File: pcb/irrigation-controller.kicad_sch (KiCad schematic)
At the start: 7 parts, among them J1 ZL262-40DG, J2 KFG-2EDGR-5.08-9P, X1 5V, X2 12V

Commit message: Update resistor values based on availability
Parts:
- R10: value 1.5K -> 1.1K; CID 100.327.80 -> 100.011.53
- R9: value 4.3K -> 3.9K; CID 100.316.93 -> 100.014.54
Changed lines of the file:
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@@
 			)
 		)
-		(property "Value" "1.5K"
+		(property "Value" "1.1K"
 			(at 227.33 107.9499 0)
 			(effects
@@
 			)
 		)
-		(property "CID" "100.327.80"
+		(property "CID" "100.011.53"
 			(at 224.79 106.68 0)
 			(effects
@@
 			)
 		)
-		(property "Value" "4.3K"
+		(property "Value" "3.9K"
 			(at 227.33 97.7899 0)
 			(effects
@@
 			)
 		)
-		(property "CID" "100.316.93"
+		(property "CID" "100.014.54"
 			(at 224.79 96.52 0)
 			(effects

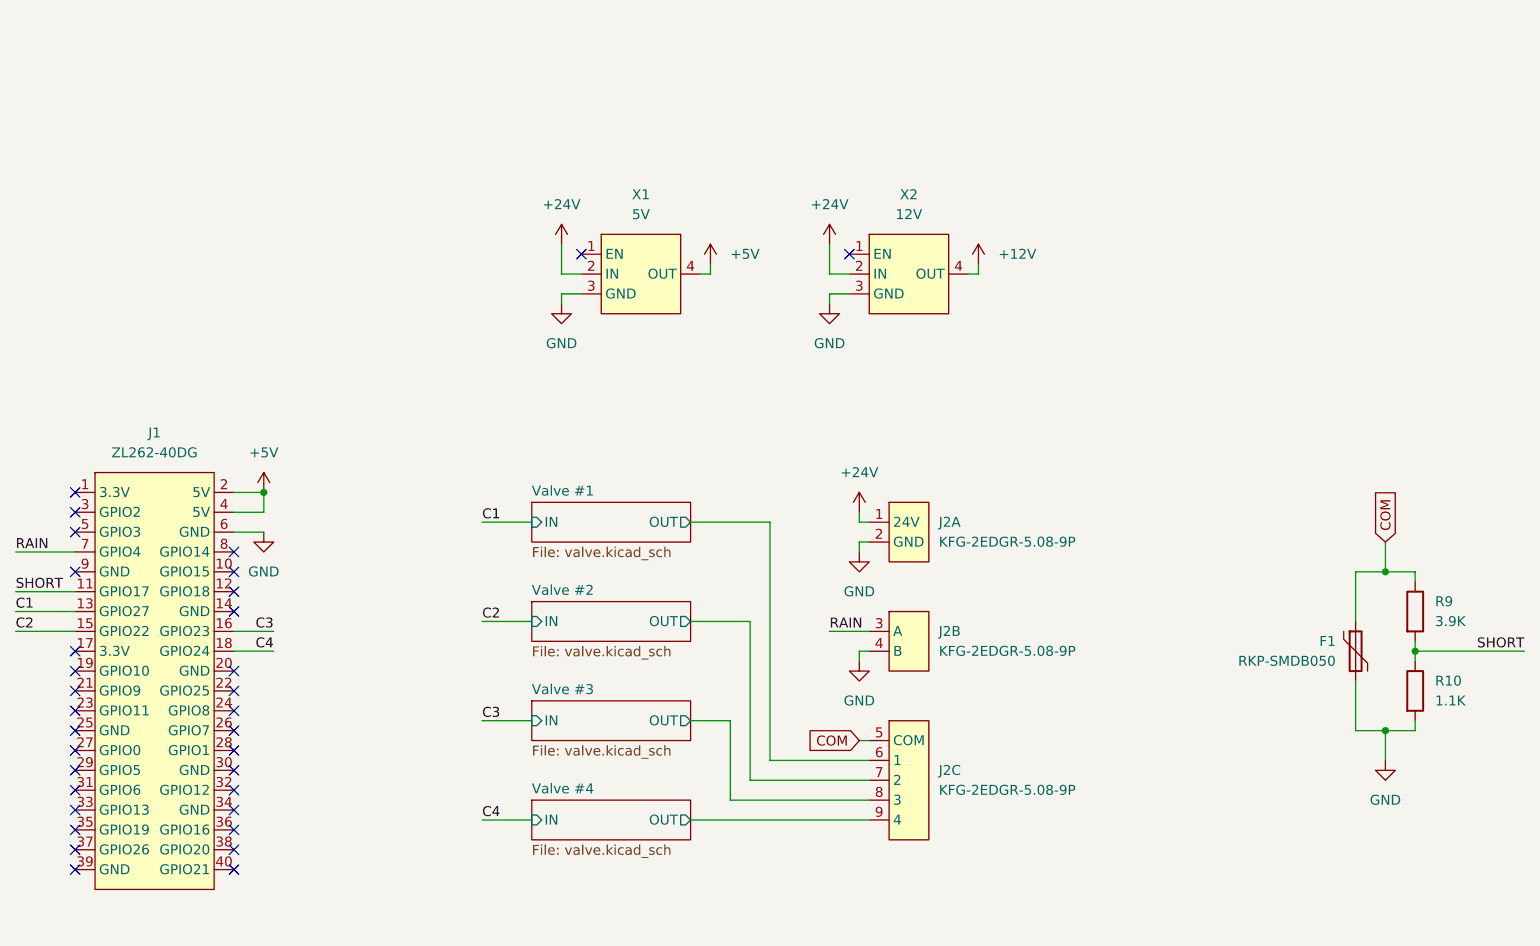
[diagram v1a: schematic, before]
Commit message: Change terminal, add another output, add hardware debouncing
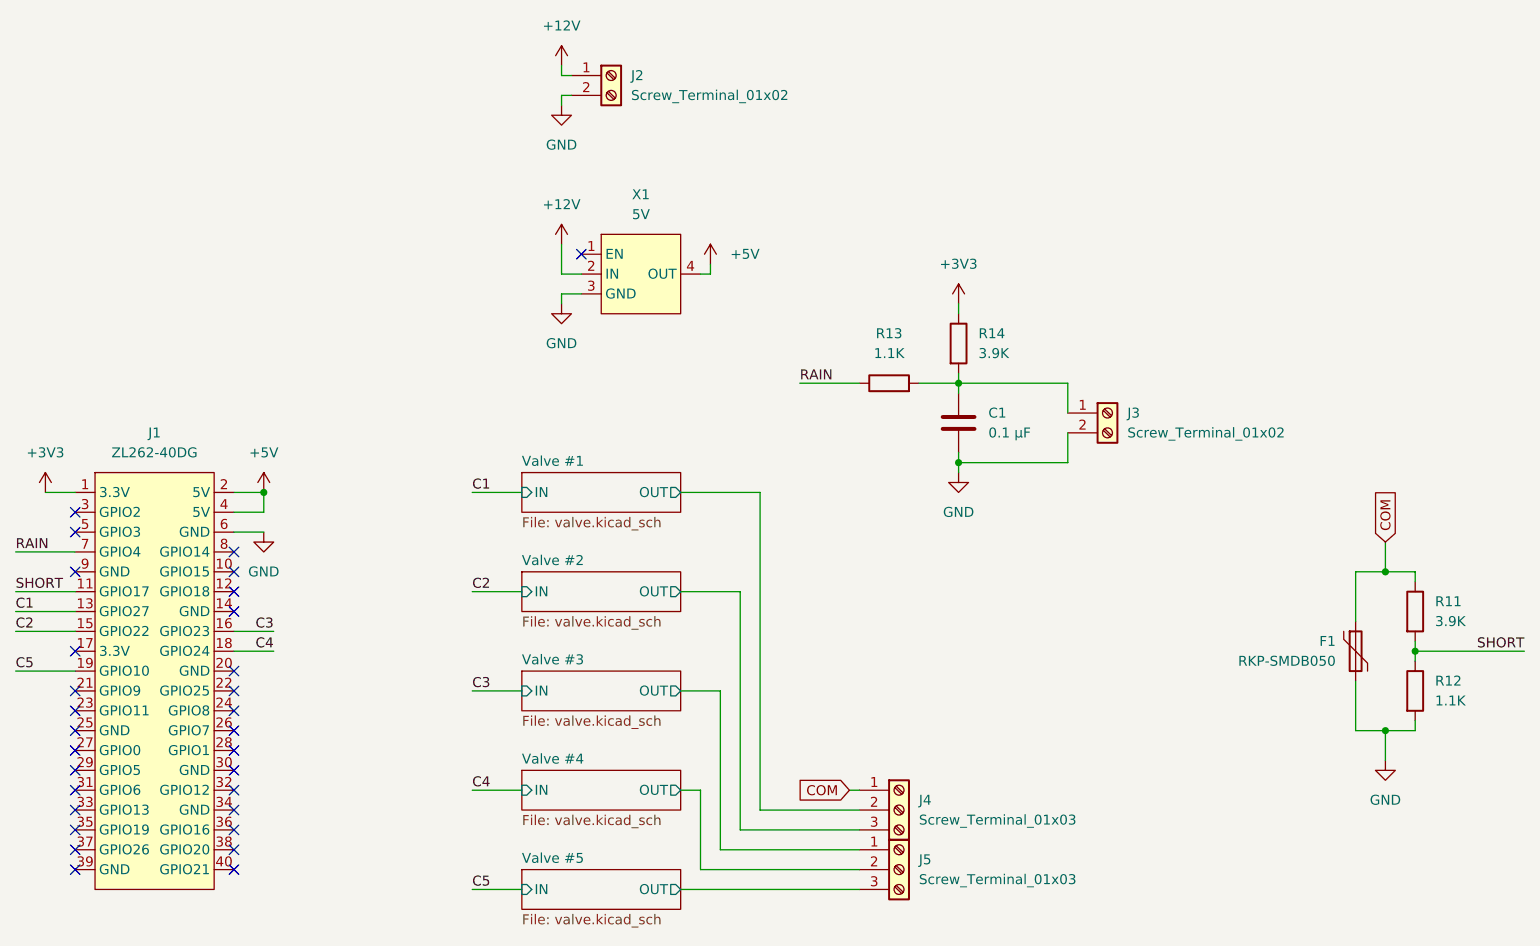
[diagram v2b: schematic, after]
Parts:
- removed J2: KFG-2EDGR-5.08-9P, Irrigation_Controller:KFG-2EDGR-5.08-9P, symbol Irrigation_Controller:Irrigation_Controller_Connector
- removed X2: 12V, Irrigation_Controller:STDN-3A24-ADJ, symbol Irrigation_Controller:STDN-3A24-ADJ
- added C1: 0.1 µF, Capacitor_SMD:C_0805_2012Metric, symbol Device:C
- added J2, J3: Screw_Terminal_01x02, Irrigation_Controller:MX5-2P-BK, symbol Connector:Screw_Terminal_01x02
- added J4, J5: Screw_Terminal_01x03, Irrigation_Controller:MX5-3P-BK, symbol Connector:Screw_Terminal_01x03
- added R13: 1.1K, Resistor_SMD:R_0805_2012Metric, symbol Device:R
- added R14: 3.9K, Resistor_SMD:R_0805_2012Metric, symbol Device:R
- renumbered R9 to R11, R10 to R12
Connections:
- net +24V is gone; now on net +12V: X1.2 (IN)
- net +12V: now also J2.1 (Pin_1)
- net COM: now also J4.1 (Pin_1)
- net GND: now also C1.2, J2.2 (Pin_2), J3.2 (Pin_2)
- net RAIN: now also R13.1
- net Valve #1/OUT: now also J4.2 (Pin_2)
- net Valve #2/OUT: now also J4.3 (Pin_3)
- net Valve #3/OUT: now also J5.1 (Pin_1)
- net Valve #4/OUT: now also J5.2 (Pin_2)
- net +3V3: now reaches J1.1 (3.3V)
- net +3V3: now also R14.1
- net C5: now reaches J1.19 (GPIO10)
- new net: C1.1, J3.1 (Pin_1), R13.2, R14.2
- new net Valve #5/OUT: J5.3 (Pin_3)
- no-connect marks 33 -> 30
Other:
- added sheet Valve #5 (valve.kicad_sch)

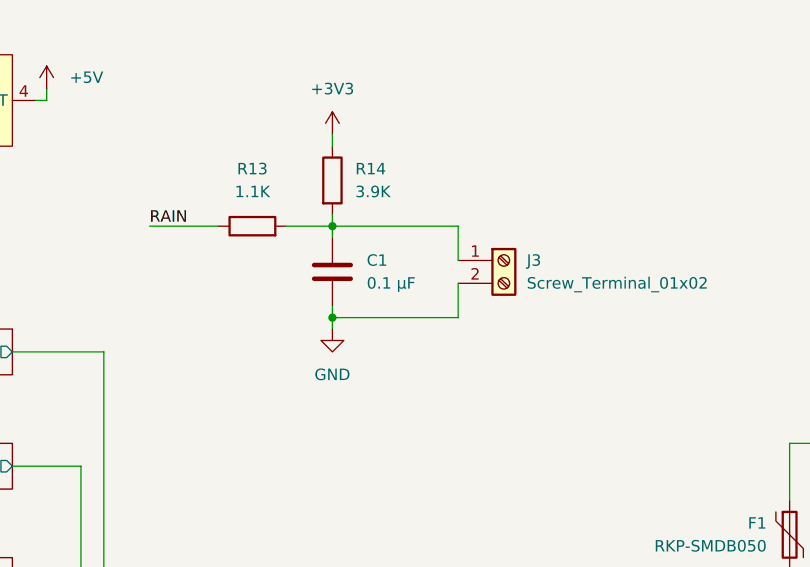
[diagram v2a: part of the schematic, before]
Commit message: Adjust components based on availability
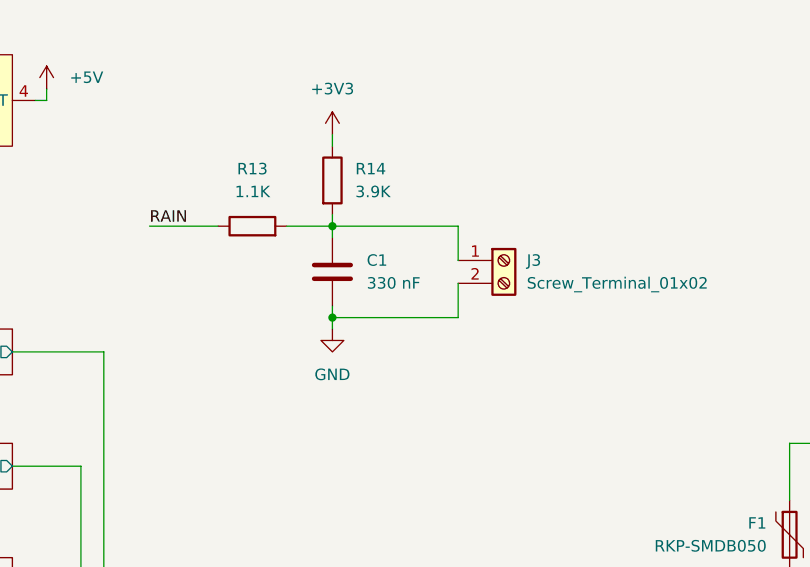
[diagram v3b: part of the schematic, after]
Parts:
- C1: value 0.1 µF -> 330 nF; CID 100.011.22 -> 100.343.20
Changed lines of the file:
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@@
 			)
 		)
-		(property "Value" "0.1 µF"
+		(property "Value" "330 nF"
 			(at 170.18 73.6599 0)
 			(effects
@@
 			)
 		)
-		(property "CID" "100.011.22"
+		(property "CID" "100.343.20"
 			(at 166.37 72.39 0)
 			(effects
